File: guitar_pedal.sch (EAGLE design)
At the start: 98 parts, among them P1 RM-065, P2 RM-065, P3 RM-065, U1 LM324NSOIC-14, U2 LM324NSOIC-14, U3 LM386N-3, U4 LM386N-3, U5 LM386N-3

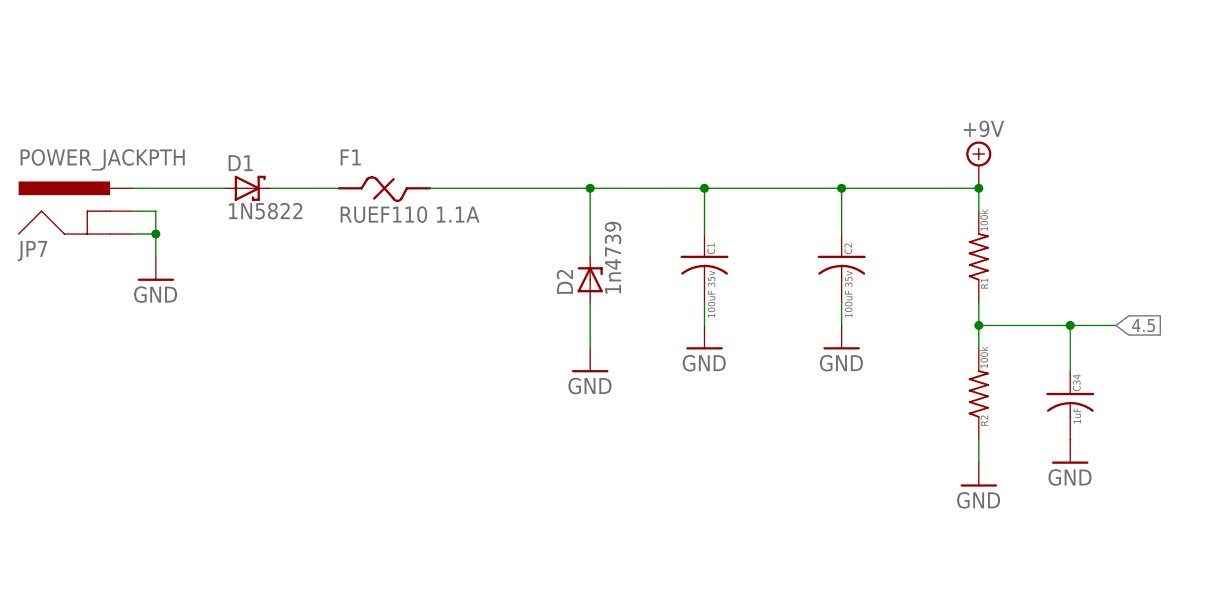
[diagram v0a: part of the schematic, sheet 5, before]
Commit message: Added most of silk screen. Added vias for debugging. Added ground vias. Added ground plane cutout to through hole components for case with no solder mask.
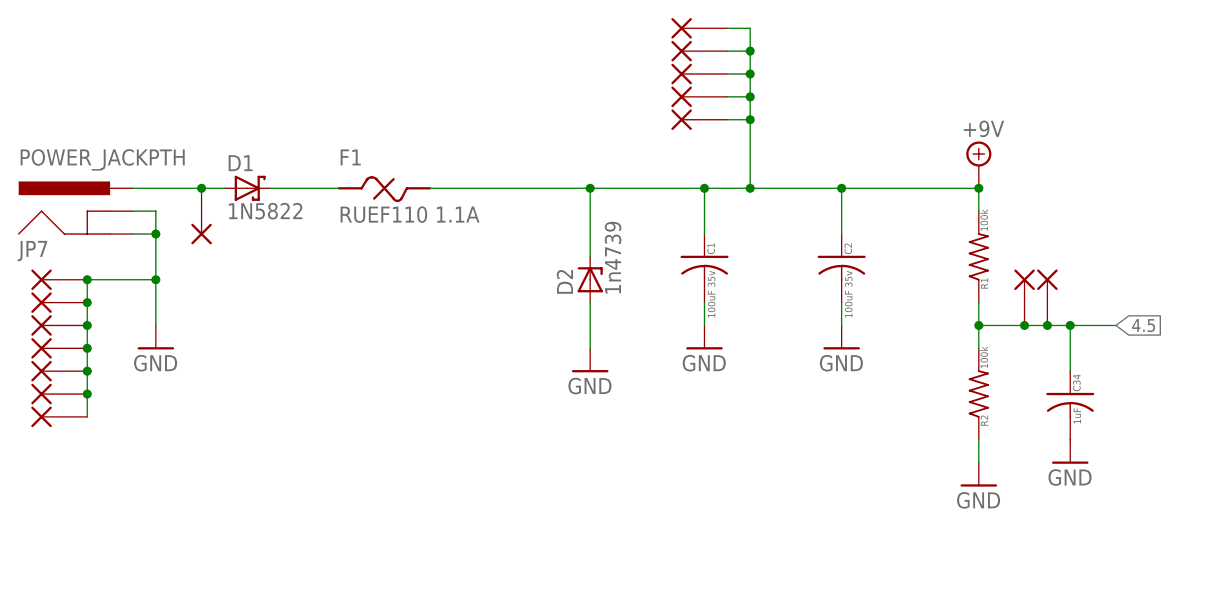
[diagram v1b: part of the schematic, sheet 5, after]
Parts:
- added V1: V+, Luke:VIA1
- added V10, V11, V12, V13, V14, V15, V16: GND, Luke:VIA1
- added V17: EQout, Luke:VIA1
- added V2: EQin, Luke:VIA1
- added V3, V4, V5, V6, V7: 9v, Luke:VIA1
- added V8, V9: 4v5, Luke:VIA1
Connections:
- net +9V: now also V3.P$1, V4.P$1, V5.P$1, V6.P$1, V7.P$1
- net 4.5: now also V8.P$1, V9.P$1
- net GND: now also V10.P$1, V11.P$1, V12.P$1, V13.P$1, V14.P$1, V15.P$1, V16.P$1
- net N$1: now also V1.P$1
- net N$12: now also V2.P$1
- net N$20: now also V17.P$1
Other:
- moved on the sheet: C14
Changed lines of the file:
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@@
 <part name="C34" library="Luke" deviceset="CAPACITOR" device="0805" value="1uF"/>
 <part name="GND40" library="supply1" deviceset="GND" device=""/>
+<part name="V1" library="Luke" deviceset="VIA1" device="" value="V+"/>
+<part name="V7" library="Luke" deviceset="VIA1" device="" value="9v"/>
+<part name="V3" library="Luke" deviceset="VIA1" device="" value="9v"/>
+<part name="V4" library="Luke" deviceset="VIA1" device="" value="9v"/>
+<part name="V5" library="Luke" deviceset="VIA1" device="" value="9v"/>
+<part name="V6" library="Luke" deviceset="VIA1" device="" value="9v"/>
+<part name="V8" library="Luke" deviceset="VIA1" device="" value="4v5"/>
+<part name="V9" library="Luke" deviceset="VIA1" device="" value="4v5"/>
+<part name="V10" library="Luke" deviceset="VIA1" device="" value="GND"/>
+<part name="V11" library="Luke" deviceset="VIA1" device="" value="GND"/>
+<part name="V12" library="Luke" deviceset="VIA1" device="" value="GND"/>
+<part name="V13" library="Luke" deviceset="VIA1" device="" value="GND"/>
+<part name="V14" library="Luke" deviceset="VIA1" device="" value="GND"/>
+<part name="V15" library="Luke" deviceset="VIA1" device="" value="GND"/>
+<part name="V16" library="Luke" deviceset="VIA1" device="" value="GND"/>
+<part name="V2" library="Luke" deviceset="VIA1" device="" value="EQin"/>
+<part name="V17" library="Luke" deviceset="VIA1" device="" value="EQout"/>
 </parts>
 <sheets>
@@
 <instance part="C29" gate="G$1" x="177.8" y="129.54"/>
 <instance part="C30" gate="G$1" x="170.18" y="129.54"/>
+<instance part="V2" gate="G$1" x="88.9" y="96.52" rot="R180"/>
 </instances>
 <busses>
@@
 <pinref part="R16" gate="G$1" pin="1"/>
 <wire x1="93.98" y1="109.22" x2="93.98" y2="104.14" width="0.1524" layer="91"/>
-<wire x1="93.98" y1="104.14" x2="93.98" y2="88.9" width="0.1524" layer="91"/>
+<wire x1="93.98" y1="104.14" x2="93.98" y2="96.52" width="0.1524" layer="91"/>
+<wire x1="93.98" y1="96.52" x2="93.98" y2="88.9" width="0.1524" layer="91"/>
 <wire x1="93.98" y1="88.9" x2="99.06" y2="88.9" width="0.1524" layer="91"/>
 <wire x1="99.06" y1="109.22" x2="93.98" y2="109.22" width="0.1524" layer="91"/>
@@
 <junction x="93.98" y="104.14"/>
 <pinref part="C9" gate="G$1" pin="NEG"/>
+<pinref part="V2" gate="G$1" pin="P$1"/>
+<junction x="93.98" y="96.52"/>
 </segment>
 </net>
@@
 <instance part="C26" gate="G$1" x="157.48" y="81.28" rot="R270"/>
 <instance part="R24" gate="G$1" x="25.4" y="121.92"/>
-<instance part="C14" gate="G$1" x="38.1" y="121.92" rot="R90"/>
+<instance part="C14" gate="G$1" x="35.56" y="121.92" rot="R90"/>
 <instance part="R25" gate="G$1" x="50.8" y="121.92"/>
 <instance part="R26" gate="G$1" x="58.42" y="114.3" rot="R270"/>
@@
 <instance part="C32" gate="G$1" x="157.48" y="139.7" rot="R270"/>
 <instance part="C33" gate="G$1" x="157.48" y="86.36" rot="R270"/>
+<instance part="V17" gate="G$1" x="43.18" y="127" rot="R90"/>
 </instances>
 <busses>
@@
 <pinref part="R24" gate="G$1" pin="2"/>
 <pinref part="C14" gate="G$1" pin="POS"/>
-<wire x1="30.48" y1="121.92" x2="35.56" y2="121.92" width="0.1524" layer="91"/>
+<wire x1="30.48" y1="121.92" x2="33.02" y2="121.92" width="0.1524" layer="91"/>
 </segment>
 </net>
@@
 <pinref part="C14" gate="G$1" pin="NEG"/>
 <pinref part="R25" gate="G$1" pin="1"/>
+<wire x1="40.64" y1="121.92" x2="43.18" y2="121.92" width="0.1524" layer="91"/>
+<pinref part="V17" gate="G$1" pin="P$1"/>
 <wire x1="43.18" y1="121.92" x2="45.72" y2="121.92" width="0.1524" layer="91"/>
+<junction x="43.18" y="121.92"/>
 </segment>
 </net>
@@
 <instances>
 <instance part="JP7" gate="G$1" x="76.2" y="114.3"/>
-<instance part="GND1" gate="1" x="81.28" y="111.76"/>
+<instance part="GND1" gate="1" x="81.28" y="104.14"/>
 <instance part="D1" gate="G$1" x="91.44" y="121.92"/>
 <instance part="D2" gate="G$1" x="129.54" y="111.76" rot="R90"/>
@@
 <instance part="C34" gate="G$1" x="182.88" y="99.06"/>
 <instance part="GND40" gate="1" x="182.88" y="91.44"/>
+<instance part="V1" gate="G$1" x="86.36" y="116.84" rot="R270"/>
+<instance part="V7" gate="G$1" x="139.7" y="139.7" rot="R180"/>
+<instance part="V3" gate="G$1" x="139.7" y="137.16" rot="R180"/>
+<instance part="V4" gate="G$1" x="139.7" y="134.62" rot="R180"/>
+<instance part="V5" gate="G$1" x="139.7" y="132.08" rot="R180"/>
+<instance part="V6" gate="G$1" x="139.7" y="129.54" rot="R180"/>
+<instance part="V8" gate="G$1" x="180.34" y="111.76" rot="R90"/>
+<instance part="V9" gate="G$1" x="177.8" y="111.76" rot="R90"/>
+<instance part="V10" gate="G$1" x="68.58" y="96.52" rot="R180"/>
+<instance part="V11" gate="G$1" x="68.58" y="99.06" rot="R180"/>
+<instance part="V12" gate="G$1" x="68.58" y="101.6" rot="R180"/>
+<instance part="V13" gate="G$1" x="68.58" y="104.14" rot="R180"/>
+<instance part="V14" gate="G$1" x="68.58" y="106.68" rot="R180"/>
+<instance part="V15" gate="G$1" x="68.58" y="109.22" rot="R180"/>
+<instance part="V16" gate="G$1" x="68.58" y="111.76" rot="R180"/>
 </instances>
 <busses>
@@
 <pinref part="JP7" gate="G$1" pin="GND"/>
 <wire x1="81.28" y1="116.84" x2="78.74" y2="116.84" width="0.1524" layer="91"/>
-<wire x1="81.28" y1="116.84" x2="81.28" y2="114.3" width="0.1524" layer="91"/>
+<wire x1="81.28" y1="116.84" x2="81.28" y2="111.76" width="0.1524" layer="91"/>
 <junction x="81.28" y="116.84"/>
 <pinref part="GND1" gate="1" pin="GND"/>
+<wire x1="81.28" y1="111.76" x2="81.28" y2="106.68" width="0.1524" layer="91"/>
+<wire x1="81.28" y1="111.76" x2="73.66" y2="111.76" width="0.1524" layer="91"/>
+<wire x1="73.66" y1="111.76" x2="73.66" y2="109.22" width="0.1524" layer="91"/>
+<junction x="81.28" y="111.76"/>
+<pinref part="V10" gate="G$1" pin="P$1"/>
+<pinref part="V11" gate="G$1" pin="P$1"/>
+<wire x1="73.66" y1="109.22" x2="73.66" y2="106.68" width="0.1524" layer="91"/>
+<wire x1="73.66" y1="106.68" x2="73.66" y2="104.14" width="0.1524" layer="91"/>
+<wire x1="73.66" y1="104.14" x2="73.66" y2="101.6" width="0.1524" layer="91"/>
+<wire x1="73.66" y1="101.6" x2="73.66" y2="99.06" width="0.1524" layer="91"/>
+<wire x1="73.66" y1="99.06" x2="73.66" y2="96.52" width="0.1524" layer="91"/>
+<junction x="73.66" y="99.06"/>
+<pinref part="V12" gate="G$1" pin="P$1"/>
+<junction x="73.66" y="101.6"/>
+<pinref part="V13" gate="G$1" pin="P$1"/>
+<junction x="73.66" y="104.14"/>
+<pinref part="V14" gate="G$1" pin="P$1"/>
+<junction x="73.66" y="106.68"/>
+<pinref part="V15" gate="G$1" pin="P$1"/>
+<junction x="73.66" y="109.22"/>
+<pinref part="V16" gate="G$1" pin="P$1"/>
+<junction x="73.66" y="111.76"/>
 </segment>
 <segment>
@@
 <segment>
 <pinref part="JP7" gate="G$1" pin="PWR"/>
-<wire x1="78.74" y1="121.92" x2="88.9" y2="121.92" width="0.1524" layer="91"/>
+<wire x1="78.74" y1="121.92" x2="86.36" y2="121.92" width="0.1524" layer="91"/>
 <pinref part="D1" gate="G$1" pin="A"/>
+<pinref part="V1" gate="G$1" pin="P$1"/>
+<wire x1="86.36" y1="121.92" x2="88.9" y2="121.92" width="0.1524" layer="91"/>
+<junction x="86.36" y="121.92"/>
 </segment>
 </net>
@@
 <wire x1="172.72" y1="109.22" x2="172.72" y2="106.68" width="0.1524" layer="91"/>
 <wire x1="172.72" y1="106.68" x2="172.72" y2="104.14" width="0.1524" layer="91"/>
-<wire x1="172.72" y1="106.68" x2="182.88" y2="106.68" width="0.1524" layer="91"/>
+<wire x1="172.72" y1="106.68" x2="177.8" y2="106.68" width="0.1524" layer="91"/>
 <junction x="172.72" y="106.68"/>
 <label x="187.96" y="106.68" size="1.4224" layer="95" xref="yes"/>
 <pinref part="C34" gate="G$1" pin="POS"/>
+<wire x1="177.8" y1="106.68" x2="180.34" y2="106.68" width="0.1524" layer="91"/>
+<wire x1="180.34" y1="106.68" x2="182.88" y2="106.68" width="0.1524" layer="91"/>
 <wire x1="182.88" y1="106.68" x2="187.96" y2="106.68" width="0.1524" layer="91"/>
 <wire x1="182.88" y1="101.6" x2="182.88" y2="106.68" width="0.1524" layer="91"/>
 <junction x="182.88" y="106.68"/>
+<pinref part="V8" gate="G$1" pin="P$1"/>
+<junction x="180.34" y="106.68"/>
+<pinref part="V9" gate="G$1" pin="P$1"/>
+<junction x="177.8" y="106.68"/>
 </segment>
 </net>
@@
 <wire x1="129.54" y1="121.92" x2="129.54" y2="114.3" width="0.1524" layer="91"/>
 <wire x1="129.54" y1="121.92" x2="142.24" y2="121.92" width="0.1524" layer="91"/>
-<wire x1="142.24" y1="121.92" x2="157.48" y2="121.92" width="0.1524" layer="91"/>
+<wire x1="142.24" y1="121.92" x2="147.32" y2="121.92" width="0.1524" layer="91"/>
+<wire x1="147.32" y1="121.92" x2="157.48" y2="121.92" width="0.1524" layer="91"/>
 <wire x1="157.48" y1="121.92" x2="172.72" y2="121.92" width="0.1524" layer="91"/>
 <wire x1="172.72" y1="121.92" x2="172.72" y2="119.38" width="0.1524" layer="91"/>
@@
 <junction x="157.48" y="121.92"/>
 <pinref part="F1" gate="G$1" pin="2"/>
-</segment>
-</net>
+<pinref part="V7" gate="G$1" pin="P$1"/>
+<wire x1="144.78" y1="139.7" x2="147.32" y2="139.7" width="0.1524" layer="91"/>
+<wire x1="147.32" y1="139.7" x2="147.32" y2="137.16" width="0.1524" layer="91"/>
+<junction x="147.32" y="121.92"/>
+<wire x1="147.32" y1="137.16" x2="147.32" y2="134.62" width="0.1524" layer="91"/>
+<wire x1="147.32" y1="134.62" x2="147.32" y2="132.08" width="0.1524" layer="91"/>
+<wire x1="147.32" y1="132.08" x2="147.32" y2="129.54" width="0.1524" layer="91"/>
+<wire x1="147.32" y1="129.54" x2="147.32" y2="121.92" width="0.1524" layer="91"/>
+<wire x1="144.78" y1="137.16" x2="147.32" y2="137.16" width="0.1524" layer="91"/>
+<junction x="147.32" y="137.16"/>
+<wire x1="144.78" y1="134.62" x2="147.32" y2="134.62" width="0.1524" layer="91"/>
+<junction x="147.32" y="134.62"/>
+<wire x1="144.78" y1="132.08" x2="147.32" y2="132.08" width="0.1524" layer="91"/>
+<junction x="147.32" y="132.08"/>
+<wire x1="144.78" y1="129.54" x2="147.32" y2="129.54" width="0.1524" layer="91"/>
+<junction x="147.32" y="129.54"/>
+<pinref part="V3" gate="G$1" pin="P$1"/>
+<pinref part="V4" gate="G$1" pin="P$1"/>
+<pinref part="V5" gate="G$1" pin="P$1"/>
+<pinref part="V6" gate="G$1" pin="P$1"/>
+</segment>
+</net>
